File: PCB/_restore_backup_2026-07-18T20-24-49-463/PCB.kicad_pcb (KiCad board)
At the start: 2 copper layers, 331.5 x 122.2 mm, 212 parts, among them J1 Conn_01x04, J2 USB, J3 Conn_01x05, U1 XC6206PxxxMR, U2 SRV05-4, U3 RP2040, U4 W25Q128JVS, Y1 Crystal_GND24

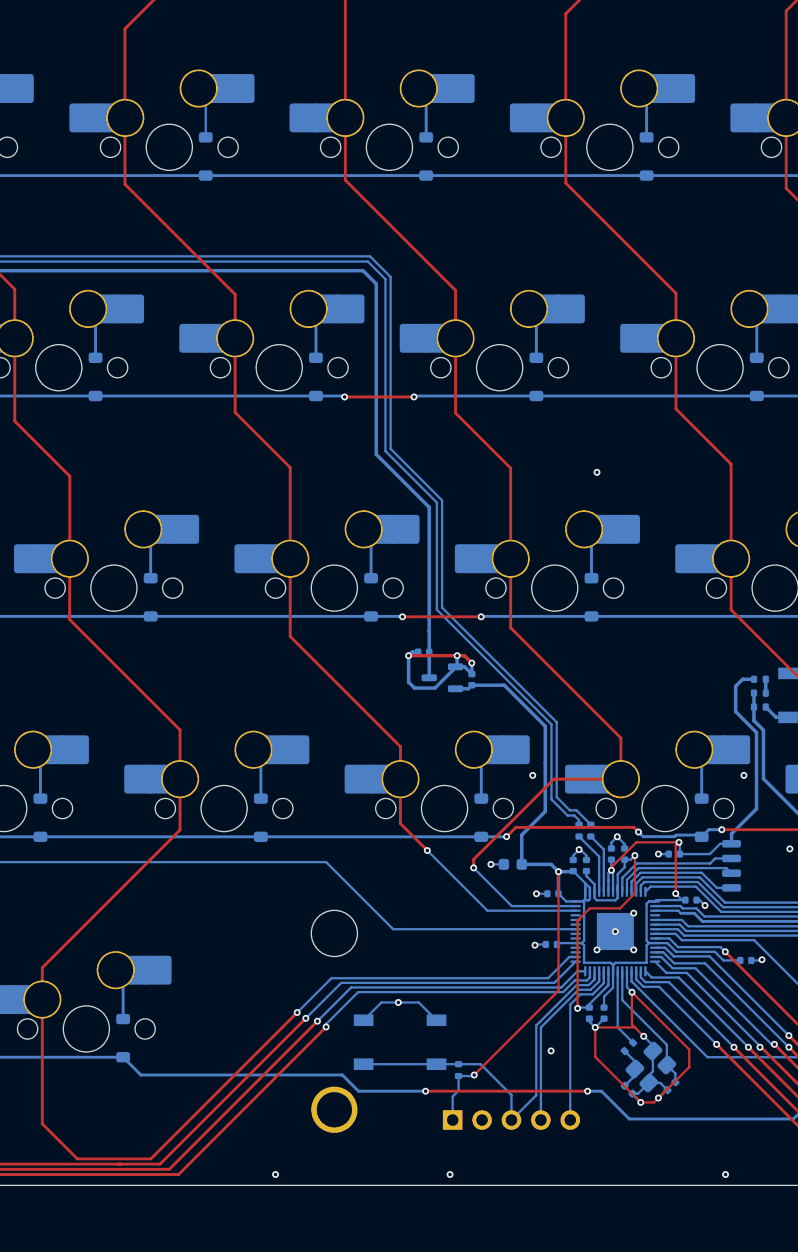
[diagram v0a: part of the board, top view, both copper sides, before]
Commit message: fixing footprints
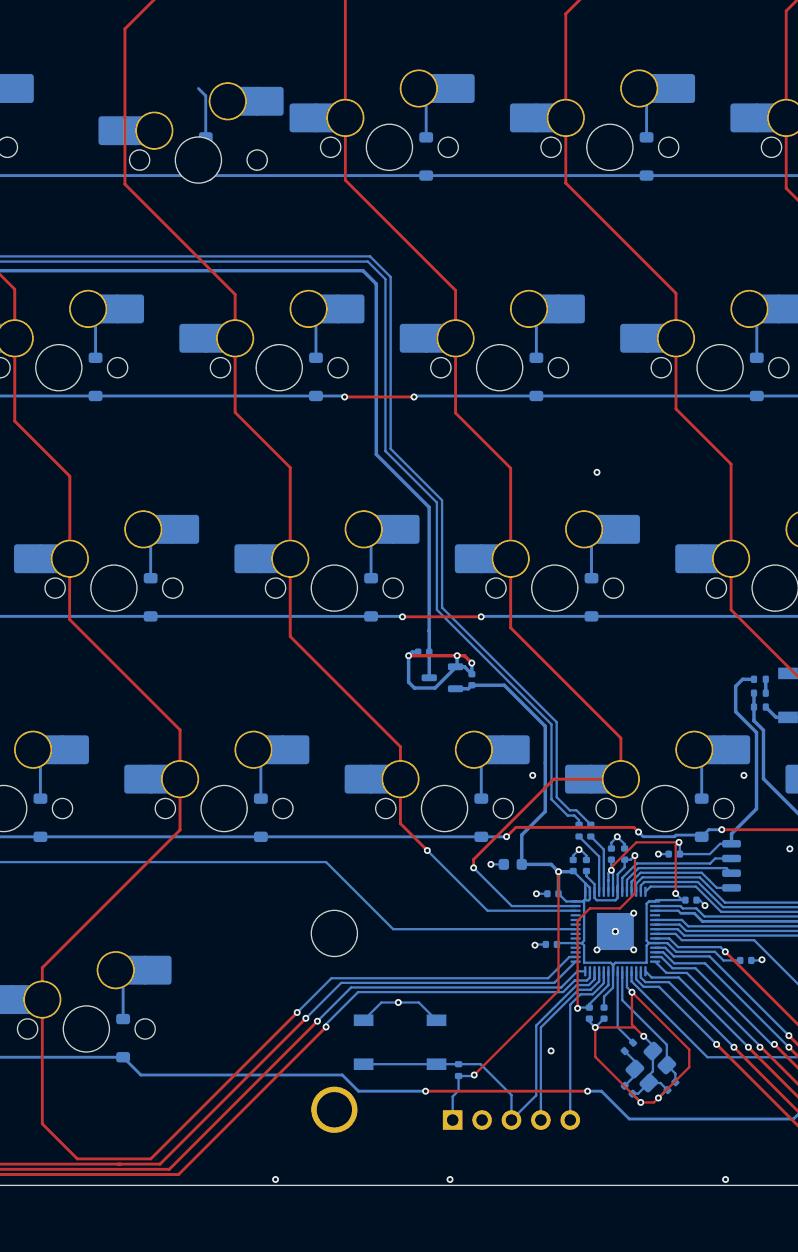
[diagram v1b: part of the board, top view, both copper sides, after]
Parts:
- moved MX19 2.75 mm to (110.6, 53.9)
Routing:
- net GND: vias 72 -> 73
